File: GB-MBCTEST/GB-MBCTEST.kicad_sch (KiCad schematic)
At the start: 17 parts

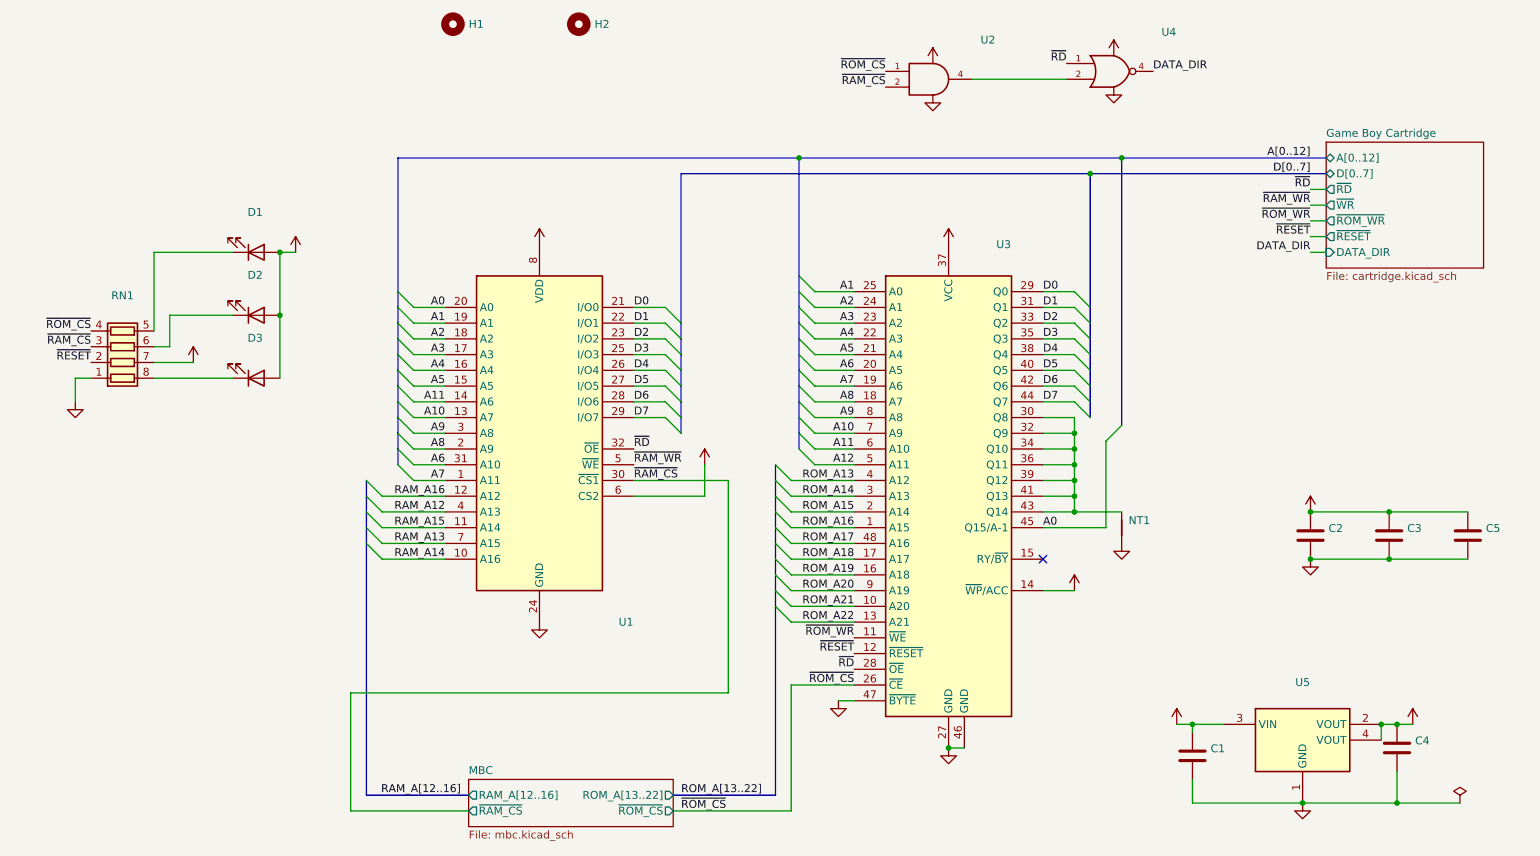
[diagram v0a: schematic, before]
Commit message: Upgrade projects to KiCad 7
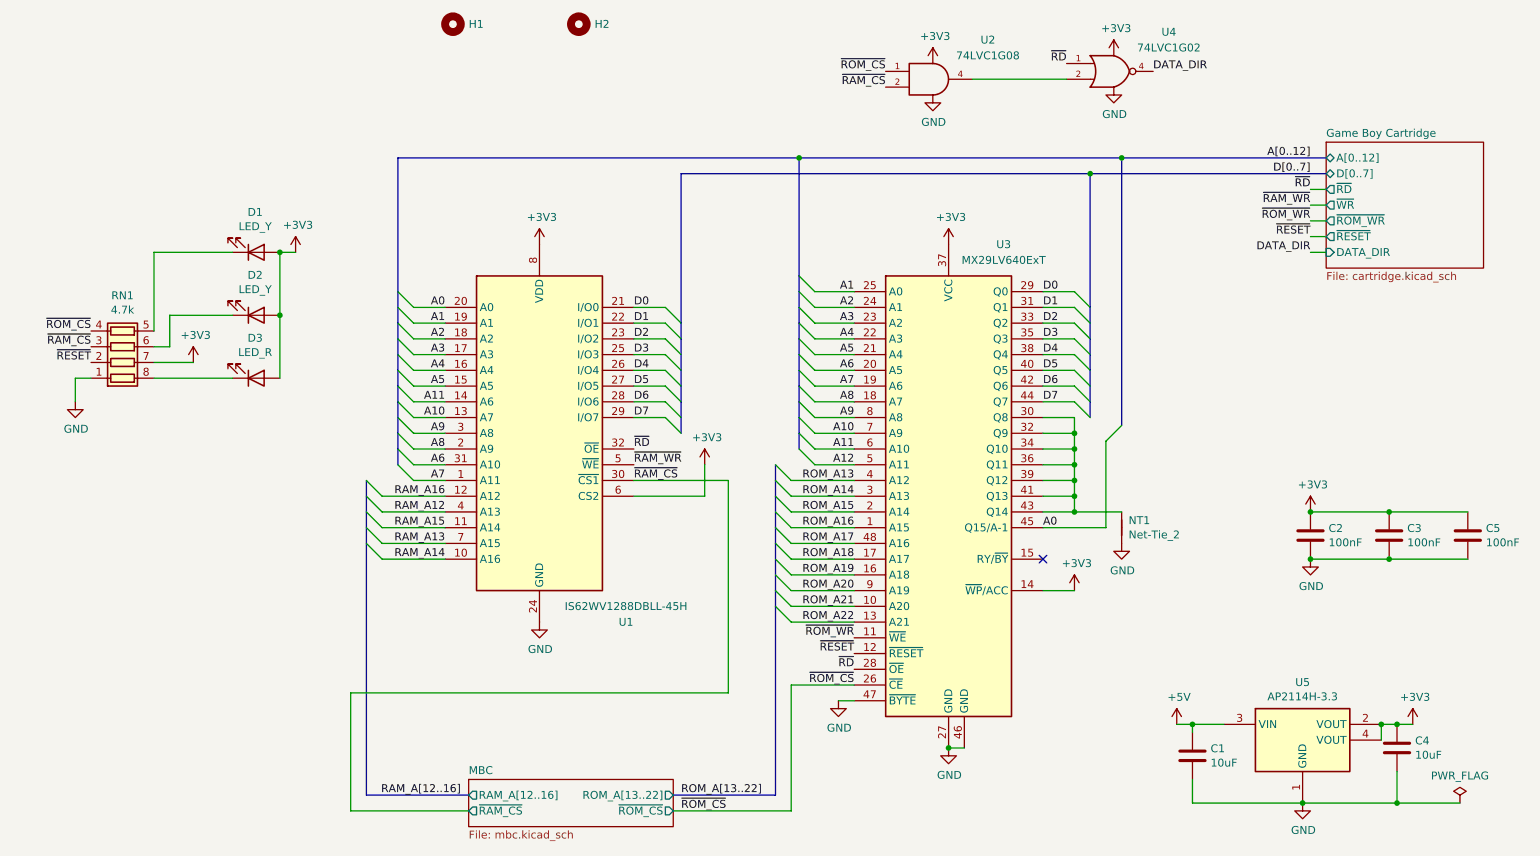
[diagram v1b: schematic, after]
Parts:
- C1, C4: value (none) -> 10uF; footprint (none) -> Capacitor_SMD:C_1206_3216Metric
- C2, C3, C5: value (none) -> 100nF; footprint (none) -> Capacitor_SMD:C_0603_1608Metric
- D1, D2: value (none) -> LED_Y; footprint (none) -> LED_SMD:LED_0603_1608Metric
- D3: value (none) -> LED_R; footprint (none) -> LED_SMD:LED_0603_1608Metric
- H1: value (none) -> DNF; footprint (none) -> Gekkio_MountingHole:MountingHole_7.2mm
- H2: value (none) -> DNF; footprint (none) -> Gekkio_MountingHole:MountingHole_2.3mm
- NT1: value (none) -> Net-Tie_2; footprint (none) -> NetTie:NetTie-2_SMD_Pad0.5mm
- RN1: value (none) -> 4.7k; footprint (none) -> Resistor_SMD:R_Array_Convex_4x0603
- U1: value (none) -> IS62WV1288DBLL-45H; footprint (none) -> Package_SO:TSOP-I-32_11.8x8mm_P0.5mm
- U2: value (none) -> 74LVC1G08; footprint (none) -> Package_TO_SOT_SMD:SOT-353_SC-70-5
- U3: value (none) -> MX29LV640ExT; footprint (none) -> Package_SO:TSOP-I-48_18.4x12mm_P0.5mm
- U4: value (none) -> 74LVC1G02; footprint (none) -> Package_TO_SOT_SMD:SOT-353_SC-70-5
- U5: value (none) -> AP2114H-3.3; footprint (none) -> Package_TO_SOT_SMD:SOT-223
